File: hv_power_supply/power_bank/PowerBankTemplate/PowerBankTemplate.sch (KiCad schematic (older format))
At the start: 43 parts, among them J1 CONN_01x02, J2 CONN_01x02, J3 USB_A, Q1 SSM3K333R, U1 USB_MicroB, U2 MCP73871T-2CCI_ML, U3 TPS61090RSAR

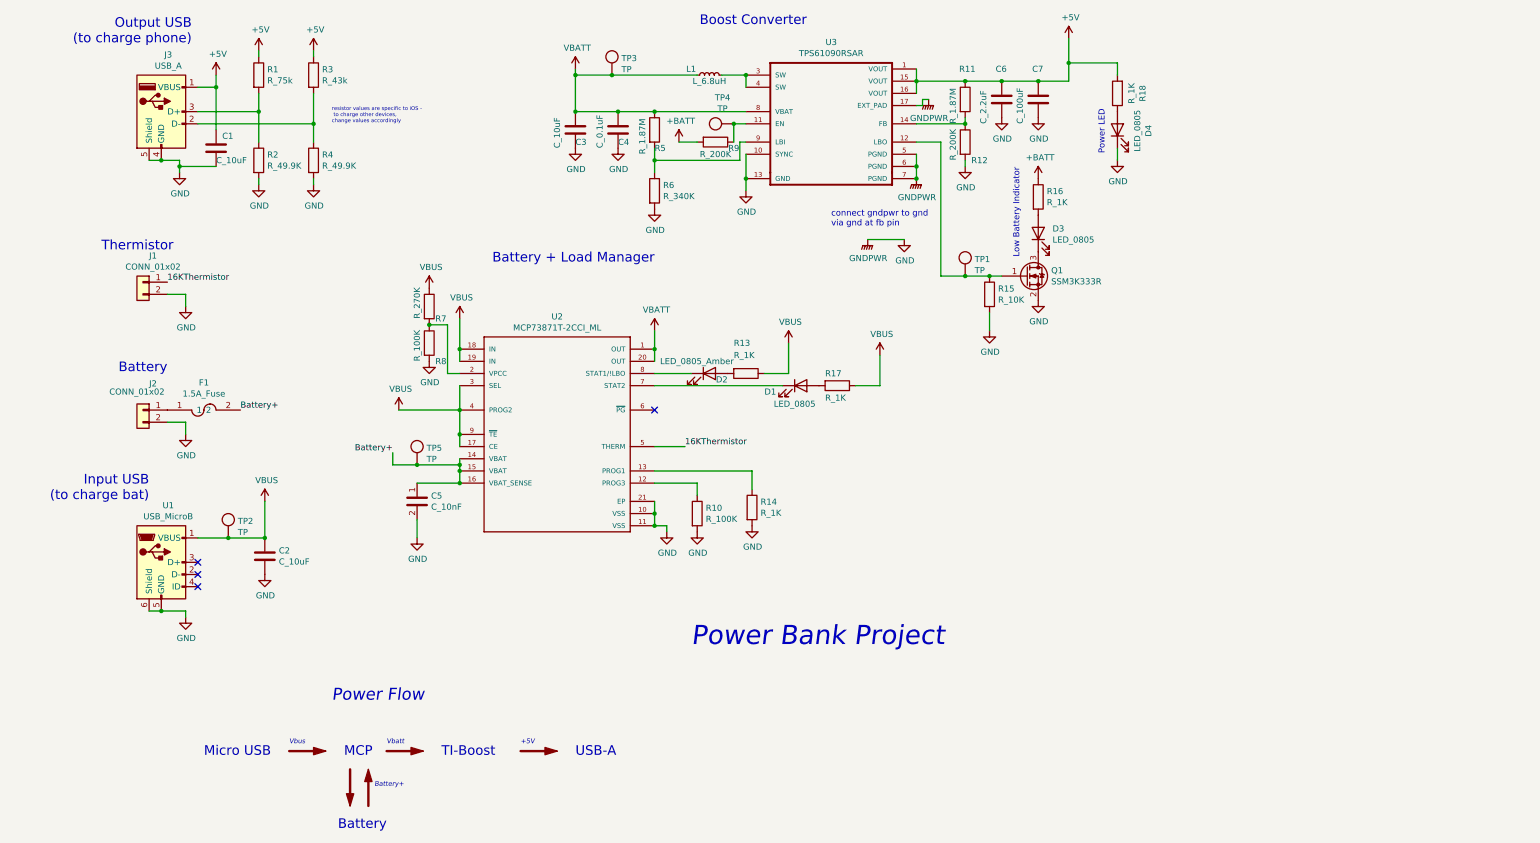
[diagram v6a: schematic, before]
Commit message: Change USB connectors on schematic
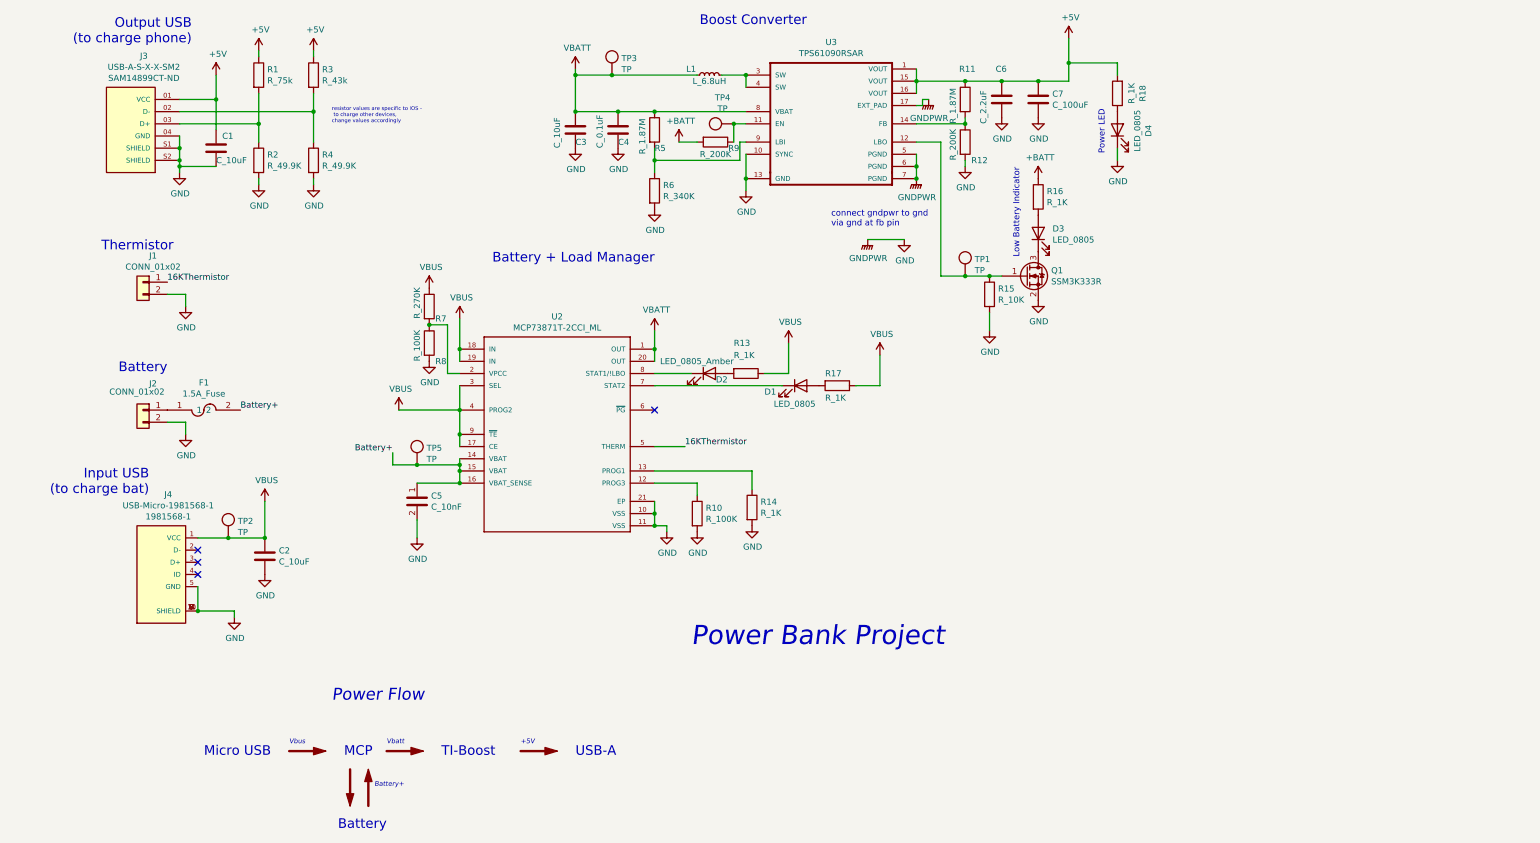
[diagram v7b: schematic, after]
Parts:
- removed J3: USB_A, symbol Connector:USB_A
- removed U1: USB_MicroB, Connectors_USB:USB_Micro-B_Molex-105017-0001, symbol formula:USB_MicroB
- added J3: USB-A-S-X-X-SM2, footprints:SAMTEC_USB-A-S-X-X-SM2, symbol formula:USB-A-S-X-X-SM2
- added J4: USB-Micro-1981568-1, footprints:TE_1981568-1, symbol formula:USB-Micro-1981568-1
- C7: footprint footprints:C_1812_OEM -> footprints:C_1812_4532Metric
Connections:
- net +5V: now also J3.01 (VCC)
- net GND: now also J3.04 (GND), J3.S1 (SHIELD), J3.S2 (SHIELD), J4.10 (SHIELD), J4.11 (SHIELD), J4.5 (GND), J4.6 (SHIELD), J4.7 (SHIELD), J4.8 (SHIELD), J4.9 (SHIELD)
- net VBUS: now also J4.1 (VCC)
- net at R3.2, R4.1: now also J3.02 (D-)
- net at R1.2, R2.1: now also J3.03 (D+)
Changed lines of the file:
@@
 $EndComp
 Connection ~ 8800 1400
-Wire Wire Line
-	8800 1400 9100 1400
 $Comp
 L power:GND #PWR029
@@
 F 3 "" H 8800 1700 50  0001 C CNN
 	1    8800 1700
-	1    0    0    -1
-$EndComp
-$Comp
-L formula:C_100uF C7
-U 1 1 5F7B6B11
-P 9100 1550
-F 0 "C7" H 9050 1800 50  0000 L CNN
-F 1 "C_100uF" V 8950 1350 50  0000 L CNN
-F 2 "footprints:C_1812_OEM" H 9100 2300 50  0001 C CNN
-F 3 "https://product.tdk.com/info/en/catalog/datasheets/mlcc_commercial_general_en.pdf" H 9300 1000 50  0001 C CNN
-F 4 "C4532X5R0J107M280KA" H 9100 2000 60  0001 C CNN "MFN"
-F 5 "445-1413-1-ND" H 9050 2150 60  0001 C CNN "MPN"
-F 6 "https://www.digikey.com/product-detail/en/tdk-corporation/C4532X5R0J107M280KA/445-1413-1-ND/567567" H 9350 1150 60  0001 C CNN "PurchasingLink"
-	1    9100 1550
 	1    0    0    -1
 $EndComp
@@
 $EndComp
 Wire Wire Line
-	9350 1400 9100 1400
-Connection ~ 9100 1400
-Wire Wire Line
-	2200 5150 2450 5150
-Wire Wire Line
 	2750 5150 2750 4850
 $Comp
@@
 NoConn ~ 2200 5350
 NoConn ~ 2200 5450
-NoConn ~ 2200 5550
+NoConn ~ 2200 5250
 $Comp
 L formula:TP TP1
@@
 $EndComp
 $Comp
-L Connector:USB_A J3
-U 1 1 5F8090A7
-P 1900 1650
-F 0 "J3" H 1957 2117 50  0000 C CNN
-F 1 "USB_A" H 1957 2026 50  0000 C CNN
-F 2 "" H 2050 1600 50  0001 C CNN
-F 3 " ~" H 2050 1600 50  0001 C CNN
-	1    1900 1650
-	1    0    0    -1
-$EndComp
-$Comp
 L power:GND #PWR04
 U 1 1 5F7F1D8F
-P 2100 5800
-F 0 "#PWR04" H 2100 5550 50  0001 C CNN
-F 1 "GND" H 2105 5627 50  0000 C CNN
-F 2 "" H 2100 5800 50  0001 C CNN
-F 3 "" H 2100 5800 50  0001 C CNN
-	1    2100 5800
-	1    0    0    -1
-$EndComp
-$Comp
-L formula:USB_MicroB U1
-U 1 1 5F7ED398
-P 1900 5350
-F 0 "U1" H 1957 5817 50  0000 C CNN
-F 1 "USB_MicroB" H 1957 5726 50  0000 C CNN
-F 2 "Connectors_USB:USB_Micro-B_Molex-105017-0001" H 1850 5700 50  0001 C CNN
-F 3 "https://www.molex.com/pdm_docs/sd/1050170001_sd.pdf" H 1850 5700 50  0001 C CNN
-F 4 "DK" H 2150 5100 50  0001 C CNN "MFN"
-F 5 "WM1399CT-ND" H 2250 5200 50  0001 C CNN "MPN"
-F 6 "https://www.digikey.com/product-detail/en/molex-llc/1050170001/WM1399CT-ND/2350885" H 2350 5300 50  0001 C CNN "PurchasingLink"
-	1    1900 5350
+P 2500 5800
+F 0 "#PWR04" H 2500 5550 50  0001 C CNN
+F 1 "GND" H 2505 5627 50  0000 C CNN
+F 2 "" H 2500 5800 50  0001 C CNN
+F 3 "" H 2500 5800 50  0001 C CNN
+	1    2500 5800
 	1    0    0    -1
 $EndComp
@@
 	2700 1200 2700 1150
 Wire Wire Line
-	2700 1500 2700 1650
-Wire Wire Line
 	2700 2200 2700 2250
 Wire Wire Line
-	2200 1650 2700 1650
-Connection ~ 2700 1650
-Wire Wire Line
-	2700 1650 2700 1900
-Wire Wire Line
 	3150 1150 3150 1200
 Wire Wire Line
-	3150 1500 3150 1750
-Wire Wire Line
 	3150 2200 3150 2250
-Wire Wire Line
-	2200 1750 3150 1750
-Connection ~ 3150 1750
-Wire Wire Line
-	3150 1750 3150 1900
 $Comp
 L power:GND #PWR01
@@
 $EndComp
 Wire Wire Line
-	1800 2050 1900 2050
-Wire Wire Line
-	2050 2050 2050 2100
-Connection ~ 1900 2050
-Wire Wire Line
-	1900 2050 2050 2050
-Wire Wire Line
-	2100 5800 2100 5750
-Wire Wire Line
-	2100 5750 1900 5750
-Connection ~ 1900 5750
-Wire Wire Line
-	1900 5750 1800 5750
+	2500 5800 2500 5750
 $Comp
 L power:+5V #PWR05
@@
 	1    0    0    -1
 $EndComp
-Wire Wire Line
-	2350 1350 2350 1450
-Wire Wire Line
-	2350 1450 2200 1450
 $Comp
 L formula:C_10uF C1
@@
 Wire Wire Line
 	2050 2100 2050 2150
-Wire Wire Line
-	2350 1800 2350 1450
-Connection ~ 2350 1450
 $Comp
 L power:VBUS #PWR08
@@
 Text Notes 1950 3800 2    79   ~ 0
 Battery
-Text Notes 1800 4850 2    79   ~ 0
+Text Notes 1800 4800 2    79   ~ 0
 Input USB\n(to charge bat)
 Text Notes 3300 6500 0    98   Italic 0
@@
 	1    0    0    -1
 $EndComp
-Connection ~ 2450 5150
-Wire Wire Line
-	2450 5150 2750 5150
 $Comp
 L formula:TP TP3
@@
 	8150 1550 8200 1550
 $Comp
-L formula:GNDPWR #PWR?
+L formula:GNDPWR #PWR0102
 U 1 1 5F8EA6AD
 P 7700 2700
-F 0 "#PWR?" H 7700 2500 50  0001 C CNN
+F 0 "#PWR0102" H 7700 2500 50  0001 C CNN
 F 1 "GNDPWR" H 7704 2546 50  0000 C CNN
 F 2 "" H 7700 2650 50  0001 C CNN
@@
 $EndComp
 $Comp
-L power:GND #PWR?
+L power:GND #PWR0103
 U 1 1 5F8EAEBF
 P 8000 2700
-F 0 "#PWR?" H 8000 2450 50  0001 C CNN
+F 0 "#PWR0103" H 8000 2450 50  0001 C CNN
 F 1 "GND" H 8005 2527 50  0000 C CNN
 F 2 "" H 8000 2700 50  0001 C CNN
@@
 Wire Wire Line
 	7700 2700 8000 2700
+Wire Wire Line
+	2200 5750 2500 5750
+Wire Wire Line
+	8800 1400 9100 1400
+$Comp
+L formula:C_100uF C7
+U 1 1 5FB5E8BF
+P 9100 1550
+F 0 "C7" H 9215 1596 50  0000 L CNN
+F 1 "C_100uF" H 9215 1505 50  0000 L CNN
+F 2 "footprints:C_1812_4532Metric" H 9100 2300 50  0001 C CNN
+F 3 "https://product.tdk.com/info/en/catalog/datasheets/mlcc_commercial_general_en.pdf" H 9300 1000 50  0001 C CNN
+F 4 "C4532X5R0J107M280KA" H 9100 2000 60  0001 C CNN "MFN"
+F 5 "445-1413-1-ND" H 9050 2150 60  0001 C CNN "MPN"
+F 6 "https://www.digikey.com/product-detail/en/tdk-corporation/C4532X5R0J107M280KA/445-1413-1-ND/567567" H 9350 1150 60  0001 C CNN "PurchasingLink"
+	1    9100 1550
+	1    0    0    -1
+$EndComp
+Connection ~ 9100 1400
+Wire Wire Line
+	9100 1400 9350 1400
+$Comp
+L formula:USB-Micro-1981568-1 J4
+U 1 1 5FB6FE94
+P 1900 5450
+F 0 "J4" H 1957 6107 50  0000 C CNN
+F 1 "USB-Micro-1981568-1" H 1957 6016 50  0000 C CNN
+F 2 "footprints:TE_1981568-1" H 1900 5450 50  0001 L BNN
+F 3 "https://www.te.com/commerce/DocumentDelivery/DDEController?Action=srchrtrv&DocNm=1981568&DocType=Customer+Drawing&DocLang=English" H 1900 5450 50  0001 L BNN
+F 4 ".65 mm[.025 in]" H 1900 5450 50  0001 L BNN "Field4"
+F 5 "Connector" H 1900 5450 50  0001 L BNN "Field5"
+F 6 "1981568-1" H 1900 5450 50  0001 L BNN "Field6"
+F 7 "1981568-1" H 1957 5925 50  0000 C CNN "MPN"
+	1    1900 5450
+	1    0    0    -1
+$EndComp
+Wire Wire Line
+	2700 1500 2700 1750
+Wire Wire Line
+	2350 1350 2350 1550
+Wire Wire Line
+	3150 1500 3150 1650
+Wire Wire Line
+	2050 1550 2350 1550
+Connection ~ 2350 1550
+Wire Wire Line
+	2350 1550 2350 1800
+Wire Wire Line
+	2050 1650 3150 1650
+Connection ~ 3150 1650
+Wire Wire Line
+	3150 1650 3150 1900
+Wire Wire Line
+	2050 1750 2700 1750
+Connection ~ 2700 1750
+Wire Wire Line
+	2700 1750 2700 1900
+Wire Wire Line
+	2050 2050 2050 2100
+$Comp
+L formula:USB-A-S-X-X-SM2 J3
+U 1 1 5FB623FD
+P 1650 1750
+F 0 "J3" H 1543 2307 50  0000 C CNN
+F 1 "USB-A-S-X-X-SM2" H 1543 2216 50  0000 C CNN
+F 2 "footprints:SAMTEC_USB-A-S-X-X-SM2" H 1650 1750 50  0001 L BNN
+F 3 "http://suddendocs.samtec.com/catalog_english/usb_a.pdf" H 1650 1750 50  0001 L BNN
+F 4 "Samtec" H 1650 1750 50  0001 L BNN "Field4"
+F 5 "Manufacturer Recommendations" H 1650 1750 50  0001 L BNN "Field5"
+F 6 "7.8 mm" H 1650 1750 50  0001 L BNN "Field6"
+F 7 "SAM14899CT-ND" H 1543 2125 50  0000 C CNN "MPN"
+	1    1650 1750
+	-1   0    0    -1
+$EndComp
+Wire Wire Line
+	2050 1850 2050 1950
+Connection ~ 2050 2050
+Connection ~ 2050 1950
+Wire Wire Line
+	2050 1950 2050 2050
+Wire Wire Line
+	2450 5150 2750 5150
+Wire Wire Line
+	2200 5150 2450 5150
+Connection ~ 2450 5150
+Wire Wire Line
+	2200 5550 2200 5750
+Connection ~ 2200 5750
 $EndSCHEMATC

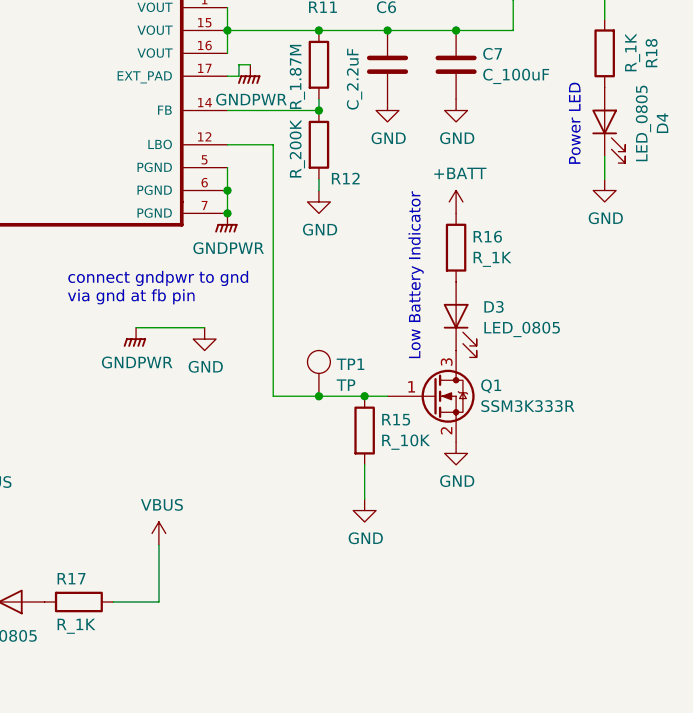
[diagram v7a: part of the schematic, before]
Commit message: Update LBO on Boost Converter of powerbank
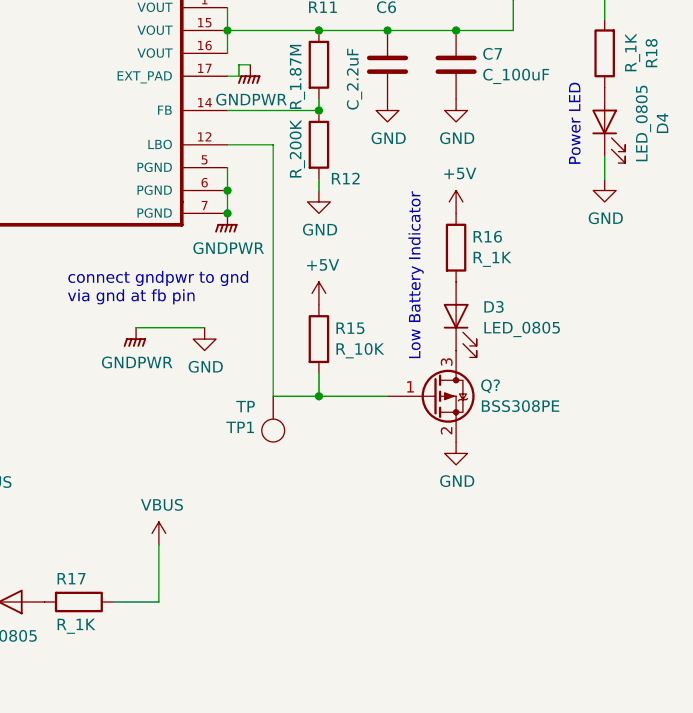
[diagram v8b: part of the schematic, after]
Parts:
- removed Q1: SSM3K333R, footprints:SOT-23F, symbol formula:SSM3K333R
- added Q?: BSS308PE, footprints:SOT-23-3_OEM, symbol formula:BSS308PE
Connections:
- net +5V: now also R15.1, R16.1
- net +BATT: no longer R16.1
- net GND: now also Q?.2 (S); no longer R15.2
- net at TP1.1 (TP), U3.12 (LBO): now also R15.2, Q?.1 (G); no longer R15.1
- net at D3.1 (K): now also Q?.3 (D)
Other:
- moved on the sheet: R15, TP1
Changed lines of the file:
@@
 	8500 2050 8500 2100
-$Comp
-L power:+BATT #PWR032
-U 1 1 5F7C320C
-P 9100 2200
-F 0 "#PWR032" H 9100 2050 50  0001 C CNN
-F 1 "+BATT" H 9115 2373 50  0000 C CNN
-F 2 "" H 9100 2200 50  0001 C CNN
-F 3 "" H 9100 2200 50  0001 C CNN
-	1    9100 2200
-	1    0    0    -1
-$EndComp
 $Comp
 L formula:R_1K R16
@@
 L formula:TP TP1
 U 1 1 5F85097E
-P 8500 2800
-F 0 "TP1" H 8578 2738 50  0000 L CNN
-F 1 "TP" H 8578 2647 50  0000 L CNN
-F 2 "footprints:tp_1.6mm" H 8400 2700 50  0001 C CNN
-F 3 "http://www.keyelco.com/product-pdf.cfm?p=1314" H 8500 2800 50  0001 C CNN
-F 4 "DK" H 8600 2900 50  0001 C CNN "MFN"
-F 5 "36-5006-ND" H 8700 3000 50  0001 C CNN "MPN"
-F 6 "https://www.digikey.com/product-detail/en/keystone-electronics/5006/36-5006-ND/255330" H 8800 3100 50  0001 C CNN "PurchasingLink"
-	1    8500 2800
-	1    0    0    -1
+P 8300 3200
+F 0 "TP1" H 8378 3138 50  0000 L CNN
+F 1 "TP" H 8378 3047 50  0000 L CNN
+F 2 "footprints:tp_1.6mm" H 8200 3100 50  0001 C CNN
+F 3 "http://www.keyelco.com/product-pdf.cfm?p=1314" H 8300 3200 50  0001 C CNN
+F 4 "DK" H 8400 3300 50  0001 C CNN "MFN"
+F 5 "36-5006-ND" H 8500 3400 50  0001 C CNN "MPN"
+F 6 "https://www.digikey.com/product-detail/en/keystone-electronics/5006/36-5006-ND/255330" H 8600 3500 50  0001 C CNN "PurchasingLink"
+	1    8300 3200
+	-1   0    0    1
 $EndComp
 Wire Wire Line
@@
 Wire Wire Line
 	9350 1250 9350 1400
-$Comp
-L formula:SSM3K333R Q1
-U 1 1 5F85122D
-P 9000 3000
-F 0 "Q1" H 9206 3046 50  0000 L CNN
-F 1 "SSM3K333R" H 9206 2955 50  0000 L CNN
-F 2 "footprints:SOT-23F" H 9200 2925 50  0001 L CIN
-F 3 "https://drive.google.com/drive/folders/0B-V-iZf33Y4GNzhDQTJZanJRbVk" H 9200 3075 50  0001 L CNN
-F 4 "DK" H 9500 3375 60  0001 C CNN "MFN"
-F 5 "SSM3K333RLFCT-ND" H 9400 3275 60  0001 C CNN "MPN"
-F 6 "https://www.digikey.com/product-detail/en/toshiba-semiconductor-and-storage/SSM3K333RLF/SSM3K333RLFCT-ND/3522391" H 9300 3175 60  0001 C CNN "PurchasingLink"
-	1    9000 3000
-	1    0    0    -1
-$EndComp
 Wire Wire Line
 	8300 1900 8300 3000
@@
 L formula:R_10K R15
 U 1 1 5F85B692
-P 8700 3150
-F 0 "R15" H 8770 3196 50  0000 L CNN
-F 1 "R_10K" H 8770 3105 50  0000 L CNN
-F 2 "footprints:R_0805_OEM" H 8630 3150 50  0001 C CNN
-F 3 "http://www.bourns.com/data/global/pdfs/CRS.pdf" H 8780 3150 50  0001 C CNN
-F 4 "DK" H 8700 3150 60  0001 C CNN "MFN"
-F 5 "CRS0805-FX-1002ELFCT-ND" H 8700 3150 60  0001 C CNN "MPN"
-F 6 "https://www.digikey.com/products/en?keywords=CRS0805-FX-1002ELFCT-ND" H 9180 3550 60  0001 C CNN "PurchasingLink"
-	1    8700 3150
-	1    0    0    -1
-$EndComp
-Connection ~ 8700 3000
-Wire Wire Line
-	8700 3000 8800 3000
+P 8500 2750
+F 0 "R15" H 8570 2796 50  0000 L CNN
+F 1 "R_10K" H 8570 2705 50  0000 L CNN
+F 2 "footprints:R_0805_OEM" H 8430 2750 50  0001 C CNN
+F 3 "http://www.bourns.com/data/global/pdfs/CRS.pdf" H 8580 2750 50  0001 C CNN
+F 4 "DK" H 8500 2750 60  0001 C CNN "MFN"
+F 5 "CRS0805-FX-1002ELFCT-ND" H 8500 2750 60  0001 C CNN "MPN"
+F 6 "https://www.digikey.com/products/en?keywords=CRS0805-FX-1002ELFCT-ND" H 8980 3150 60  0001 C CNN "PurchasingLink"
+	1    8500 2750
+	1    0    0    -1
+$EndComp
 Connection ~ 8500 3000
-Wire Wire Line
-	8500 3000 8700 3000
 $Comp
 L formula:CONN_01x02 J2
@@
 Battery+
 Wire Wire Line
-	8700 3300 8700 3450
-$Comp
-L power:GND #PWR028
-U 1 1 5F85BCCC
-P 8700 3450
-F 0 "#PWR028" H 8700 3200 50  0001 C CNN
-F 1 "GND" H 8705 3277 50  0000 C CNN
-F 2 "" H 8700 3450 50  0001 C CNN
-F 3 "" H 8700 3450 50  0001 C CNN
-	1    8700 3450
-	1    0    0    -1
-$EndComp
-Wire Wire Line
 	5950 4950 5950 5050
 Wire Wire Line
@@
 	2200 5550 2200 5750
 Connection ~ 2200 5750
+Wire Wire Line
+	8500 3000 8800 3000
+Wire Wire Line
+	8500 3000 8500 2900
+$Comp
+L power:+5V #PWR?
+U 1 1 60224A48
+P 8500 2600
+F 0 "#PWR?" H 8500 2450 50  0001 C CNN
+F 1 "+5V" H 8515 2773 50  0000 C CNN
+F 2 "" H 8500 2600 50  0001 C CNN
+F 3 "" H 8500 2600 50  0001 C CNN
+	1    8500 2600
+	1    0    0    -1
+$EndComp
+$Comp
+L power:+5V #PWR?
+U 1 1 6022A291
+P 9100 2200
+F 0 "#PWR?" H 9100 2050 50  0001 C CNN
+F 1 "+5V" H 9115 2373 50  0000 C CNN
+F 2 "" H 9100 2200 50  0001 C CNN
+F 3 "" H 9100 2200 50  0001 C CNN
+	1    9100 2200
+	1    0    0    -1
+$EndComp
+$Comp
+L formula:BSS308PE Q?
+U 1 1 6022BB7A
+P 9000 3000
+F 0 "Q?" H 9206 3046 50  0000 L CNN
+F 1 "BSS308PE" H 9206 2955 50  0000 L CNN
+F 2 "footprints:SOT-23-3_OEM" H 9200 3100 50  0001 C CNN
+F 3 "https://www.infineon.com/dgdl/BSS308PE_Rev2.03.pdf?folderId=db3a304314dca38901154a72e3951a65&fileId=db3a304330f686060131099c80400073" H 9200 3050 50  0001 C CNN
+F 4 "DK" H 9000 3000 60  0001 C CNN "MFN"
+F 5 "BSS308PEH6327XTSA1CT-ND" H 9000 3000 60  0001 C CNN "MPN"
+F 6 "https://www.digikey.com/products/en/discrete-semiconductor-products/transistors-fets-mosfets-single/278?k=bss308pe&k=&pkeyword=bss308pe&pv7=2&pv1989=0&sf=0&quantity=&ColumnSort=0&page=1&stock=1&datasheet=1&pageSize=25" H 9600 3450 60  0001 C CNN "PurchasingLink"
+	1    9000 3000
+	1    0    0    -1
+$EndComp
 $EndSCHEMATC
